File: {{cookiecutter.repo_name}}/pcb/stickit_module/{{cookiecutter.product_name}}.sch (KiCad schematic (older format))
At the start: 2 parts

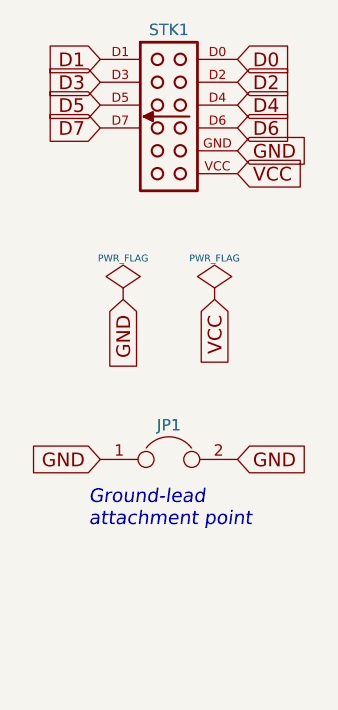
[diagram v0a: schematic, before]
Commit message: Added VCC access point to StickIt! module template. * Added template for RPi HAT. * Added template for StickIt! motherboard.
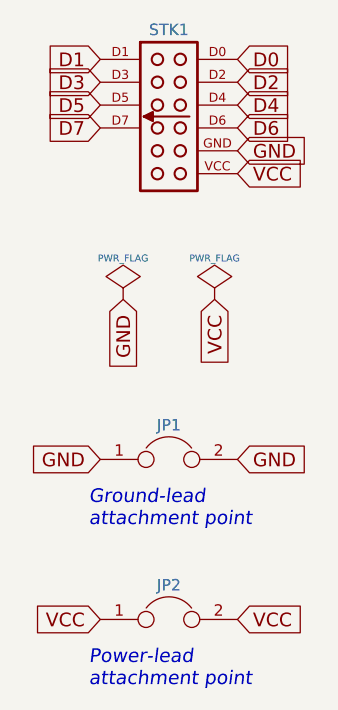
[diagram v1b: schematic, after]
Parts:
- added JP2: JUMPER, XESS:HDR_1x2, symbol JUMPER
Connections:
- net VCC: now also JP2.1, JP2.2
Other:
- note added: "Power-lead\nattachment point"
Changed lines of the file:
@@
 LIBS:memory
 LIBS:xilinx
-LIBS:special
 LIBS:microcontrollers
 LIBS:dsp
@@
 35 C9 DE 37 33 58 FE 1E 9A CA D8 EF A3 F1 DE 43 CB DE 47 23 AC F8 1E 5A 56 24 B8 8B EC 3D 74 03
 F0 6F B2 D3 0A 2F 53 9F A2 E2 FE 3F 79 73 7C 38 8D AC 56 91 00 00 00 00 49 45 4E 44 AE 42 60 82
-3A
+30
 EndData
 $EndBitmap
@@
 Text Notes 4700 4550 0    60   Italic 0
 Ground-lead\nattachment point
+$Comp
+L JUMPER JP2
+U 1 1 57179D3C
+P 5050 4950
+F 0 "JP2" H 5050 5100 50  0000 C CNN
+F 1 "JUMPER" H 5050 4870 50  0001 C CNN
+F 2 "XESS:HDR_1x2" H 5050 4950 60  0001 C CNN
+F 3 "" H 5050 4950 60  0000 C CNN
+	1    5050 4950
+	1    0    0    -1
+$EndComp
+Text GLabel 4750 4950 0    60   Input ~ 0
+VCC
+Text GLabel 5350 4950 2    60   Input ~ 0
+VCC
+Text Notes 4700 5250 0    60   Italic 0
+Power-lead\nattachment point
 $EndSCHEMATC
